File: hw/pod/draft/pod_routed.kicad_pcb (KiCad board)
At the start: 4 copper layers, 20 x 10 mm, 52 parts, among them J1 TestPoint_Pad_D1.0mm, J2 TestPoint_Pad_D1.0mm, J3 TestPoint_Pad_D1.0mm, J4 TestPoint_Pad_D1.0mm, J5 TestPoint_Pad_D1.0mm, J6 TestPoint_Pad_D1.0mm, Q1 SOT1216_L1.1-W1.0-P0.35-BL-EP, Q2 SOT1216_L1.1-W1.0-P0.35-BL-EP, SW1 SW-SMD_L3.0-W2.0-LS3.5, U1 QFN-48-1EP_7x7mm_P0.5mm_EP5.6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, U2 Knowles_LGA-5_3.5x2.65mm, U3 SOT-23-5, U4 X2SON-4_L1.0-W1.0-P0.65-TL-EP, Y1 FC-135R_L3.2-W1.5

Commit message: Draft route run 2: 0 DRC errors, 8 connections unrouted; render script; 150-pass rerun in progress
Co-Authored-By: Claude Opus 5.5 <noreply@anthropic.com>
Claude-Session: https://claude.ai/code/session_016uLR3rVesNK6FmgR7vwByF
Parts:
- moved R1 1.12 mm to (15.8, 0.80)
- moved L1 0.60 mm to (17.4, 8.60)
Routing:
- net MIC_DATA: track 15.8 -> 0.00 mm, vias 2 -> 0
- net VBAT_SENSE: track 17.9 -> 3.10 mm, vias 2 -> 0
- net VLXSMPS: track 13.3 -> 0.00 mm, vias 3 -> 0
- net GND: track 106.4 -> 119.7 mm
- net N$1: track 8.65 -> 0.00 mm, vias 2 -> 0
- net N$2: track 17.2 -> 24.8 mm
- net VDD11: track 35.1 -> 29.9 mm, vias 3 -> 2
- net BTN: track 19.1 -> 23.6 mm, vias 2 -> 3
- net NRST: track 12.6 -> 8.09 mm
- net SWCLK: track 17.3 -> 21.0 mm
- net LSE_OUT: track 5.35 -> 8.20 mm
- net GA_N: track 15.0 -> 17.8 mm
- net CHG_STAT: track 25.7 -> 23.7 mm, vias 3 -> 2
- net GA_P: track 6.35 -> 8.10 mm
- net GB_P: track 8.72 -> 7.03 mm, vias 1 -> 2
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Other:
- outline, holes or cut-outs redrawn

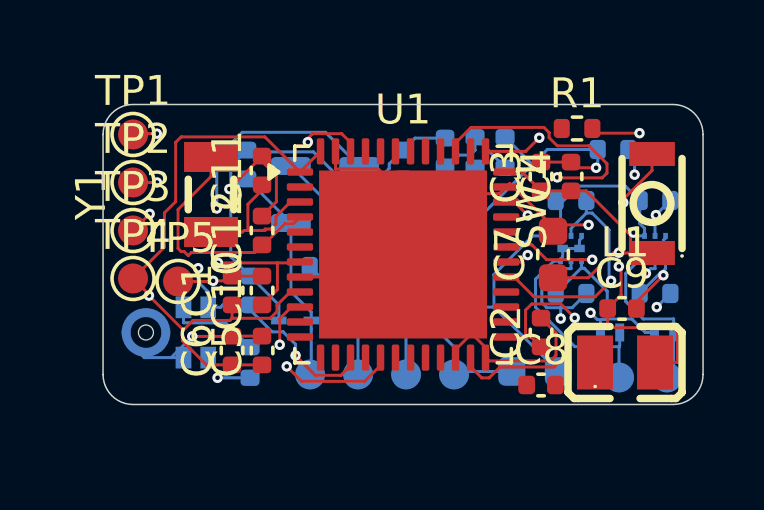
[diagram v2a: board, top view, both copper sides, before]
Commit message: Pod board fully autorouted on 20x11.5 mm (0 unconnected, DRC clean at JLC min); design review v1 complete
Co-Authored-By: Claude Opus 5.5 <noreply@anthropic.com>
Claude-Session: https://claude.ai/code/session_016uLR3rVesNK6FmgR7vwByF
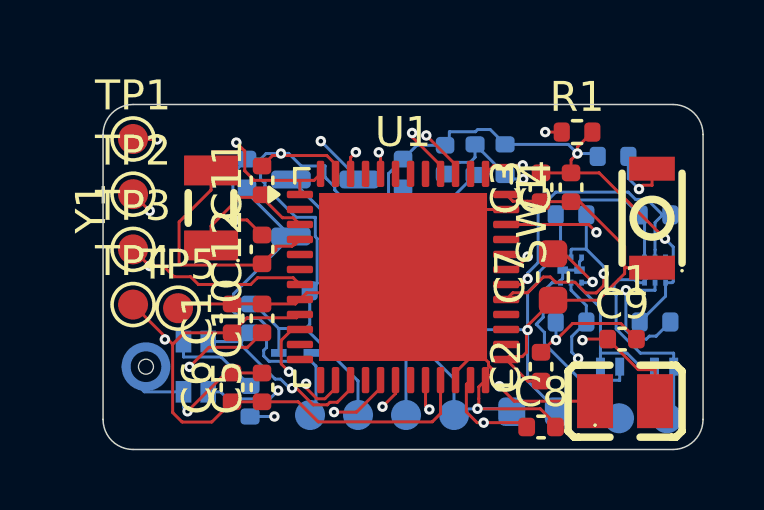
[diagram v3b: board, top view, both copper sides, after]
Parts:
- moved C8 1.40 mm to (14.6, 10.8)
- moved J1 1.36 mm to (17.2, 10.5)
- moved J2 1.36 mm to (18.8, 10.5)
- moved J3 1.35 mm to (6.90, 10.3)
- moved J4 1.35 mm to (8.50, 10.3)
- moved J5 1.35 mm to (10.1, 10.3)
- moved J6 1.35 mm to (11.7, 10.3)
- moved C14 1.34 mm to (14.4, 10.2)
- moved L1 1.29 mm to (17.4, 9.89)
- moved R2 1.29 mm to (4.90, 9.89)
- moved C5 1.23 mm to (5.30, 9.43)
- moved C6 1.23 mm to (4.30, 9.43)
- moved C2 1.14 mm to (14.6, 8.74)
- moved D1 1.14 mm to (16.9, 8.74)
- moved D2 1.14 mm to (18.7, 8.74)
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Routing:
- net VBAT_SENSE: track 3.10 -> 26.0 mm, vias 0 -> 2
- net MIC_DATA: track 0.00 -> 16.2 mm, vias 0 -> 2
- net GB_N: track 2.54 -> 15.2 mm
- net GND: track 119.7 -> 109.9 mm
- net N$2: track 24.8 -> 16.0 mm
- net N$1: track 0.00 -> 7.12 mm, vias 0 -> 2
- net VLXSMPS: track 0.00 -> 7.08 mm, vias 0 -> 2
- net CHG_STAT: track 23.7 -> 17.1 mm
- net VDD11: track 29.9 -> 23.4 mm, vias 2 -> 3
- net +3V0: track 68.6 -> 74.8 mm, vias 4 -> 3
- net SWCLK: track 21.0 -> 15.2 mm
- net SWDIO: track 15.2 -> 20.4 mm
- net NRST: track 8.09 -> 13.0 mm
- net BTN: track 23.6 -> 19.2 mm, vias 3 -> 2
- net VBUS: track 7.42 -> 11.7 mm
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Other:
- board size 20 x 10 mm -> 20 x 11.5 mm
